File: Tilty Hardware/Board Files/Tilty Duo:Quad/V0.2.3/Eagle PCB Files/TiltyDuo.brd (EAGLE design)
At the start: 38.1 x 50.8 mm, 43 parts, among them U1 TEENSY_3.0_OUTER-PINS28-DIP_S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, U2 HC-09_BREAKOUT, U3 MPL3115A2LGA8, U4 LM2931, U5 MPU-6050, U6 HMC5883LSMD, U7 24LC08BT

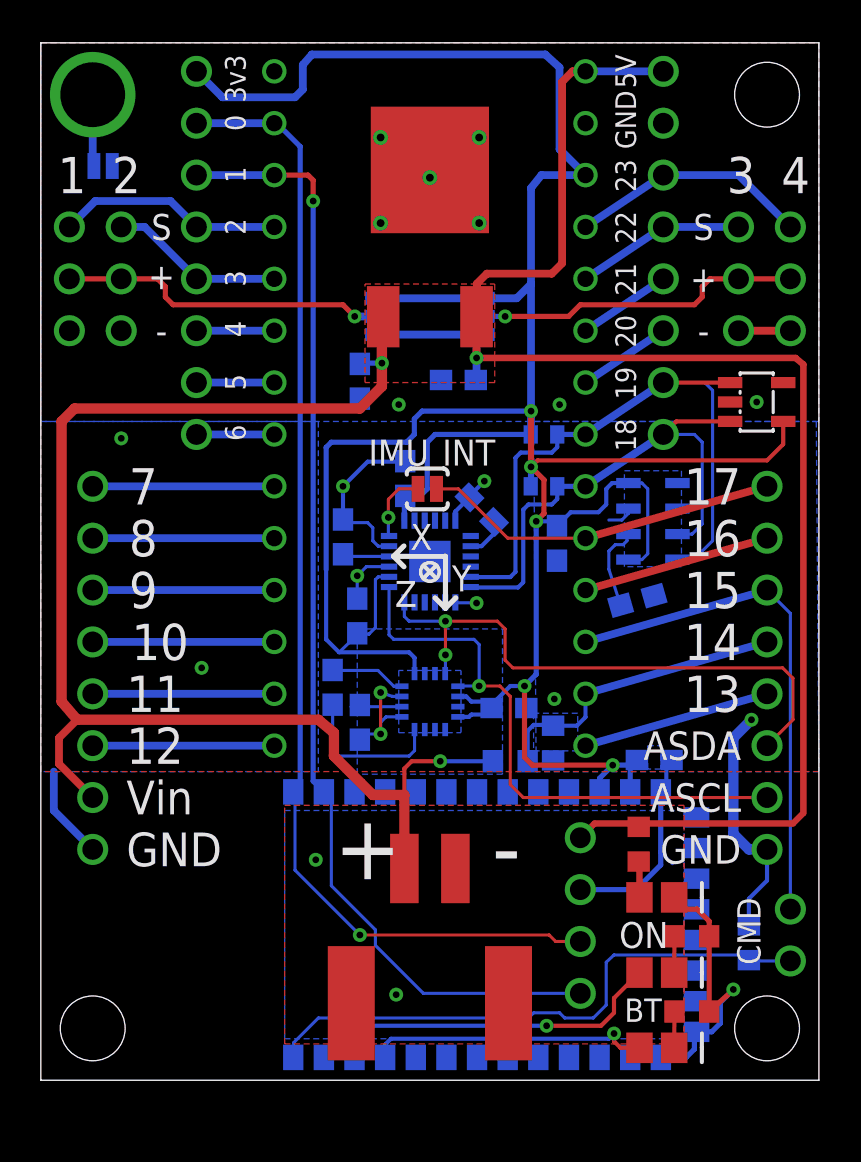
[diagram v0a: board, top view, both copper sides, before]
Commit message: PCB hardware update
Tilty Duo/Quad v0.2.3 PCB added with minor changes.
Tilty Quad BOM updated for v0.2.2
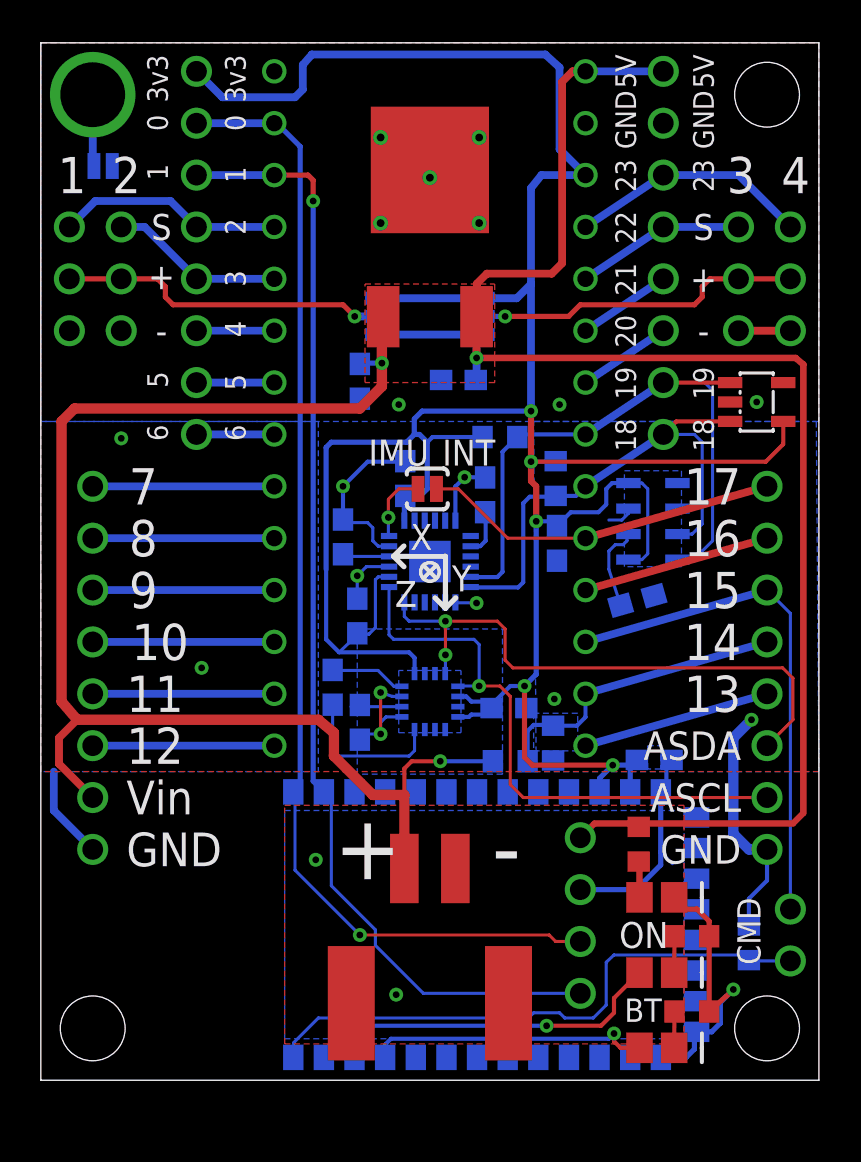
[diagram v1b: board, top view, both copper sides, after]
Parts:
- R1, R2: device resistor:R0402 -> resistor:R0603
- moved R1 2.16 mm to (22.5, 31.5)
- moved C3 0.74 mm to (21.8, 28.7), turned to 90 degrees
- moved R2 0.69 mm to (25.2, 29.5), turned to 90 degrees
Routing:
- net TEENSY_3V3: track 149.1 -> 146.2 mm
- net GND: track 66.9 -> 67.7 mm

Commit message: Updated dual motor driver and Tilty Duo/Quad PCBs, added a copuple experimental arduino programs
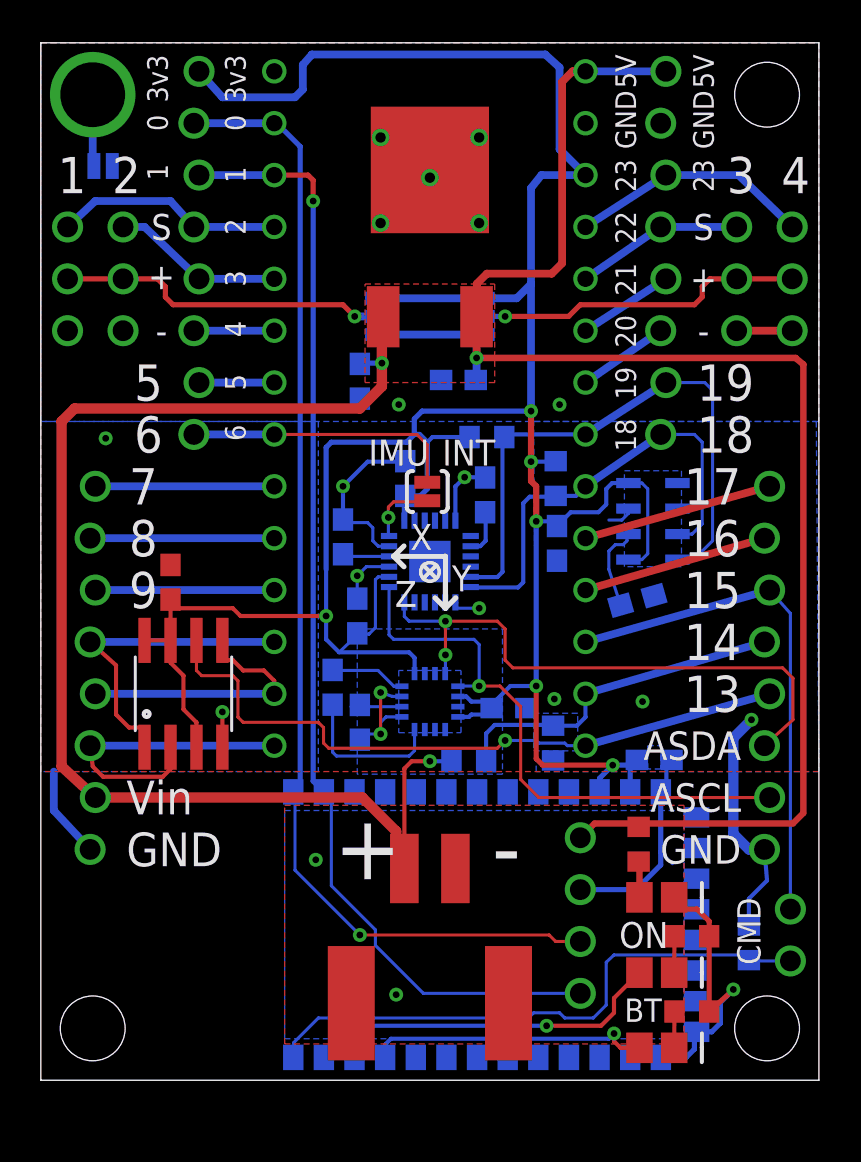
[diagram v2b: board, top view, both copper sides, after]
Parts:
- added C13: 0.1uF, resistor:C0603
- JP1, JP2, JP5, JP6: device pinhead:1X08_NO_SS -> pinhead:1X08_NO_SS_LOCKING
- JP3, JP7: device pinhead:2X03_NO_SS -> pinhead:2X03_NO_SS_LOCK
- U7: value 24LC08BT -> SPI_FLASH-X25XXSMD; device microchip:SOT23-5L -> SparkFun-DigitalIC:SO08
- moved U7 31.5 mm to (6.99, 18.9), turned to 0 degrees
- moved R5 2.03 mm to (21.0, 15.6)
- moved R1 0.63 mm to (21.8, 31.5)
- moved MPU_INT 0.13 mm to (18.9, 28.8), turned to 270 degrees
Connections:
- removed net N$13: JP2.5, U1.P$12
- removed net N$14: JP2.4, U1.P$13
- removed net N$15: JP2.3, U1.P$14
- removed net N$9: JP1.1, U1.P$8
- new net CS: JP2.5, U1.P$12, U7.1
- new net MISO: JP2.3, U1.P$14, U7.2
- new net MOSI: JP2.4, U1.P$13, U7.5
- new net SCK: JP6.4, U1.P$28, U7.6
- net GND: now also C13.1, U7.4; no longer U7.2, U7.5
- net MPU_INT: now also JP1.1, U1.P$8; no longer JP6.8, U1.P$24
- net N$10: now also JP6.8, U1.P$24; no longer JP6.4, U1.P$28
- net SCL: no longer U7.1
- net SDA: no longer U7.3
- net TEENSY_3V3: now also C13.2, U7.3, U7.7, U7.8; no longer U7.4
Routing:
- net SCK: track 0.00 -> 33.2 mm, vias 0 -> 1
- net CS: track 0.00 -> 15.8 mm
- net MISO: track 0.00 -> 15.3 mm
- net MOSI: track 0.00 -> 13.3 mm
- net N$15: track 8.89 -> 0.00 mm
- net N$14: track 8.89 -> 0.00 mm
- net N$13: track 8.89 -> 0.00 mm
- net MPU_INT: track 17.5 -> 13.5 mm
- net N$9: track 3.81 -> 0.00 mm
- net SDA: track 25.5 -> 22.0 mm
- net VBATT: track 68.2 -> 64.8 mm
- net SCL: track 31.9 -> 29.1 mm
- net TEENSY_3V3: track 146.2 -> 148.4 mm, vias 5 -> 6
- net GND: track 67.7 -> 69.9 mm
- net BATT_SENSE: track 15.2 -> 17.0 mm
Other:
- board text added: "V0.2.3"
- board text removed: "V0.2.2"

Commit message: Slightly improved Tilty Duo/Quad PCB traces
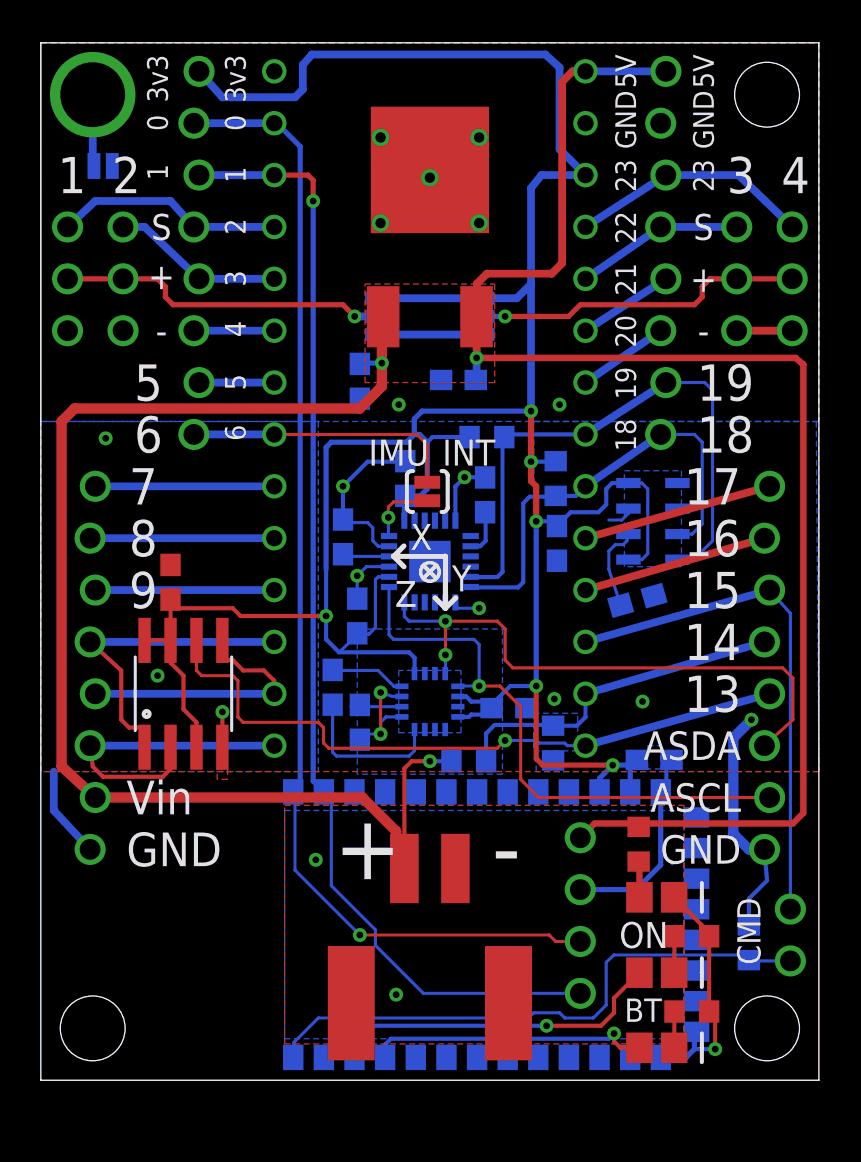
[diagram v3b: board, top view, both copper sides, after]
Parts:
- C12, C5, C9: value 1uF -> 0.1uF
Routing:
- net GND: track 69.9 -> 67.8 mm, vias 21 -> 22
- added copper zone on layer 1, net N$9
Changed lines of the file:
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@@
 <layer number="49" name="Reference" color="7" fill="1" visible="no" active="yes"/>
 <layer number="50" name="dxf" color="7" fill="1" visible="no" active="no"/>
-<layer number="51" name="tDocu" color="6" fill="1" visible="yes" active="yes"/>
-<layer number="52" name="bDocu" color="7" fill="1" visible="no" active="yes"/>
+<layer number="51" name="tDocu" color="15" fill="1" visible="yes" active="yes"/>
+<layer number="52" name="bDocu" color="7" fill="1" visible="yes" active="yes"/>
 <layer number="53" name="tGND_GNDA" color="7" fill="9" visible="no" active="no"/>
 <layer number="54" name="bGND_GNDA" color="1" fill="9" visible="no" active="no"/>
@@
 </element>
 <element name="C4" library="resistor" package="C0603" value="0.1uF" x="15.621" y="34.2265" smashed="yes" rot="MR270"/>
-<element name="C5" library="resistor" package="C0603" value="1uF" x="20.447" y="34.29" smashed="yes" rot="MR0"/>
+<element name="C5" library="resistor" package="C0603" value="0.1uF" x="20.447" y="34.29" smashed="yes" rot="MR0"/>
 <element name="U1" library="My Parts" package="28-DIP" value="TEENSY_3.0_OUTER-PINS28-DIP_SOCKET" x="19.05" y="32.893">
 <attribute name="COST" value="0.28" x="19.05" y="32.893" size="1.778" layer="27" display="off"/>
@@
 <element name="D2" library="SparkFun-LED" package="LED-0805" value="RED" x="30.1625" y="8.9535" smashed="yes"/>
 <element name="R4" library="resistor" package="R0603" value="150" x="29.2735" y="11.557" smashed="yes" rot="R270"/>
-<element name="C9" library="resistor" package="C0603" value="1uF" x="30.0355" y="15.6845" smashed="yes" rot="MR180">
+<element name="C9" library="resistor" package="C0603" value="0.1uF" x="30.0355" y="15.6845" smashed="yes" rot="MR180">
 <attribute name="RATED_VOLTAGE" value="2" x="30.0355" y="15.6845" size="1.778" layer="28" rot="MR180" display="off"/>
 </element>
@@
 <attribute name="VALUE" x="14.605" y="36.1315" size="0.4064" layer="28" rot="MR90"/>
 </element>
-<element name="C12" library="resistor" package="C0603" value="1uF" x="25.273" y="26.289" smashed="yes" rot="MR90"/>
+<element name="C12" library="resistor" package="C0603" value="0.1uF" x="25.273" y="26.289" smashed="yes" rot="MR90"/>
 <element name="U7" library="SparkFun-DigitalIC" package="SO08" value="SPI_FLASH-X25XXSMD" x="6.985" y="18.923" smashed="yes">
 <attribute name="VALUE" x="5.715" y="18.288" size="0.4064" layer="27"/>
@@
 <wire x1="30.6315" y1="15.4305" x2="30.8855" y2="15.6845" width="0.2032" layer="16"/>
 <contactref element="R8" pad="1"/>
-<wire x1="32.727" y1="7.0485" x2="32.727" y2="3.3655" width="0.254" layer="1"/>
-<wire x1="32.727" y1="7.0485" x2="32.727" y2="7.786" width="0.254" layer="1"/>
-<wire x1="32.727" y1="7.786" x2="32.131" y2="8.382" width="0.254" layer="1"/>
-<wire x1="32.131" y1="8.382" x2="30.988" y2="8.382" width="0.254" layer="1"/>
 <wire x1="34.671" y1="7.581" x2="34.671" y2="8.89" width="0.2032" layer="16"/>
 <wire x1="34.671" y1="8.89" x2="35.56" y2="9.779" width="0.2032" layer="16"/>
@@
 <wire x1="17.2085" y1="18.796" x2="16.637" y2="18.9865" width="0.1524" layer="16"/>
 <wire x1="16.637" y1="18.9865" x2="16.637" y2="16.9545" width="0.1524" layer="1"/>
-<via x="33.909" y="4.445" extent="1-16" drill="0.3302"/>
-<wire x1="33.909" y1="4.445" x2="33.9335" y2="4.445" width="0.254" layer="1"/>
-<wire x1="33.9335" y1="4.445" x2="32.727" y2="3.3655" width="0.254" layer="1"/>
-<wire x1="32.11" y1="2.37" x2="32.85" y2="2.37" width="0.254" layer="16"/>
-<wire x1="32.85" y1="2.37" x2="33.274" y2="2.794" width="0.254" layer="16"/>
-<wire x1="33.274" y1="2.794" x2="33.274" y2="3.81" width="0.254" layer="16"/>
-<wire x1="33.274" y1="3.81" x2="33.909" y2="4.445" width="0.254" layer="16"/>
 <wire x1="15.4695" y1="16.7005" x2="15.621" y2="16.676" width="0.254" layer="16"/>
 <polygon width="0.1524" layer="16">
@@
 <wire x1="21.463" y1="23.114" x2="20.3" y2="23.114" width="0.1524" layer="16"/>
 <wire x1="20.3" y1="23.114" x2="20.3" y2="23.4" width="0.1524" layer="16"/>
+<via x="5.715" y="19.812" extent="1-16" drill="0.3302"/>
+<wire x1="32.727" y1="3.3655" x2="32.727" y2="7.0485" width="0.2032" layer="1"/>
+<wire x1="32.727" y1="7.0485" x2="32.727" y2="7.239" width="0.2032" layer="1"/>
+<wire x1="32.727" y1="7.239" x2="31.0125" y2="8.9535" width="0.2032" layer="1"/>
+<via x="33.02" y="1.524" extent="1-16" drill="0.3302"/>
+<wire x1="33.02" y1="1.524" x2="33.02" y2="3.0725" width="0.2032" layer="1"/>
+<wire x1="33.02" y1="3.0725" x2="32.727" y2="3.3655" width="0.2032" layer="1"/>
+<wire x1="33.02" y1="1.524" x2="32.004" y2="1.524" width="0.2032" layer="16"/>
 </signal>
 <signal name="SCL" class="4">
@@
 <contactref element="JP2" pad="5"/>
 <wire x1="2.413" y1="21.463" x2="11.43" y2="21.463" width="0.381" layer="16"/>
-<wire x1="2.413" y1="21.463" x2="3.683" y2="20.32" width="0.2032" layer="1"/>
-<wire x1="3.683" y1="20.32" x2="3.683" y2="17.907" width="0.2032" layer="1"/>
-<wire x1="3.683" y1="17.907" x2="4.318" y2="17.272" width="0.2032" layer="1"/>
+<wire x1="2.413" y1="21.463" x2="3.937" y2="20.066" width="0.2032" layer="1"/>
+<wire x1="3.937" y1="20.066" x2="3.937" y2="17.653" width="0.2032" layer="1"/>
+<wire x1="3.937" y1="17.653" x2="4.318" y2="17.272" width="0.2032" layer="1"/>
+<wire x1="5.08" y1="17.272" x2="5.08" y2="16.3068" width="0.2032" layer="1"/>
 <wire x1="4.318" y1="17.272" x2="5.08" y2="17.272" width="0.2032" layer="1"/>
-<wire x1="5.08" y1="17.272" x2="5.08" y2="16.3068" width="0.2032" layer="1"/>
 </signal>
 <signal name="SCK">
@@
 <wire x1="26.67" y1="26.543" x2="35.687" y2="29.083" width="0.381" layer="1"/>
 </signal>
+<signal name="N$9">
+<polygon width="0.1524" layer="1" pour="cutout">
+<vertex x="8.636" y="15.24"/>
+<vertex x="9.144" y="15.24"/>
+<vertex x="9.144" y="14.732"/>
+<vertex x="8.636" y="14.732"/>
+</polygon>
+</signal>
 </signals>

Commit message: Updated Tilty Duo/Quad v0.2.3 prototype
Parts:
- D1: value GREEN -> RED
- D2: value RED -> GREEN
- R3: value 68 -> 180
- R4: value 150 -> 68
- moved R4 8.58 mm to (31.6, 3.30), turned to 0 degrees
- moved D2 7.43 mm to (30.0, 1.52)
- moved R3 4.44 mm to (29.2, 10.6), turned to 0 degrees
- moved R8 3.63 mm to (31.6, 6.99)
- moved D1 3.62 mm to (30.0, 8.89)
- moved D3 3.50 mm to (30.0, 5.08)
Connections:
- net GRN_LED renamed RED_LED
- removed net N$17: D2.1, R4.2
- new net N$13: D2.2, R4.1
- net 5V: now also D2.1; no longer R4.1
- net GND: now also R4.2; no longer D2.2
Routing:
- net RED_LED: track 16.5 -> 20.9 mm
- net 5V: track 79.5 -> 83.4 mm
- net YEL_LED: track 13.8 -> 16.6 mm
- net GND: track 67.8 -> 70.5 mm
- net N$13: track 0.00 -> 1.80 mm
- net N$17: track 1.79 -> 0.00 mm
- net RX1: vias 1 -> 2
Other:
- board text added: "PWR"
- board text removed: "ON"
